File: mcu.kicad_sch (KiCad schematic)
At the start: 14 parts, among them SW301 Reset, SW302 Boot, U301 ESP32-S3-WROOM-1-N8

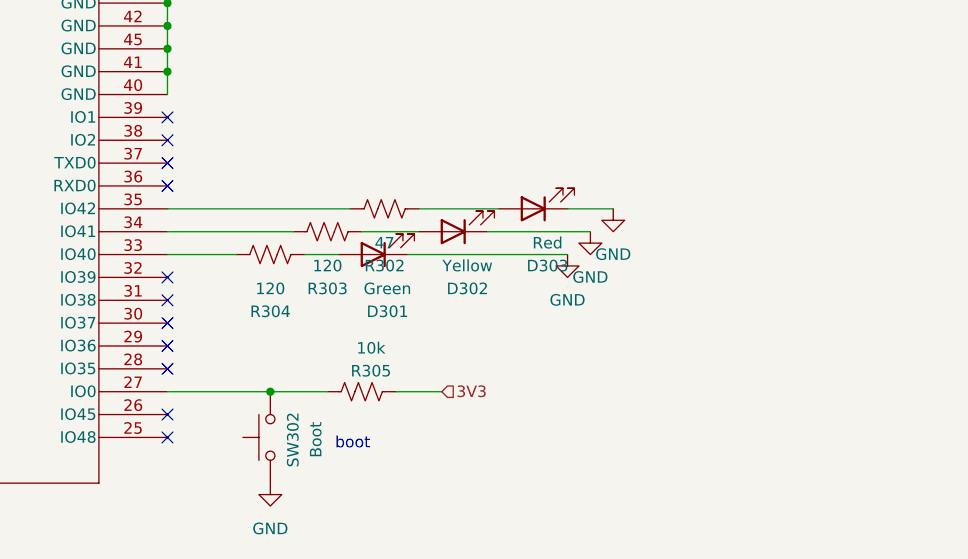
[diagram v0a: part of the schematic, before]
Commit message: added stoplight button
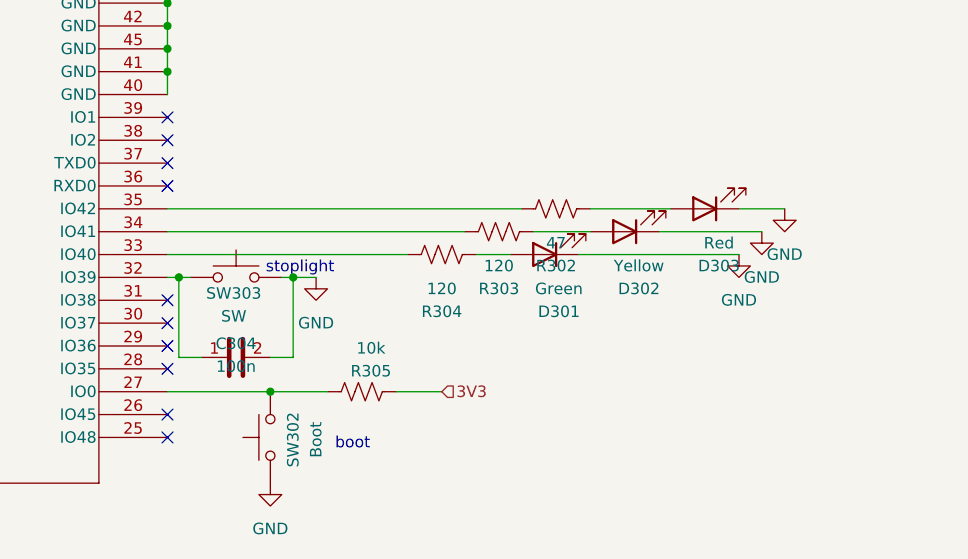
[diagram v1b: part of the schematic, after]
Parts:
- added C304: 100n, Capacitor_SMD:C_0603_1608Metric_Pad1.08x0.95mm_HandSolder, symbol bfr_capacitors:06035C104KAT2A
- added SW303: SW, Button_Switch_SMD:SW_Push_SPST_NO_Alps_SKRK, symbol bfr_actuators:Generic_Pushbutton
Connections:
- net GND: now also C304.2, SW303.2
- net at U301.32 (IO39): now also C304.1, SW303.1
- no-connect marks 30 -> 29
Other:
- note added: "stoplight"
- moved on the sheet: D301, D302, D303, R302, R303, R304
